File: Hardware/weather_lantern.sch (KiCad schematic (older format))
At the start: 3 parts

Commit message: Added sensors
Added sensors.
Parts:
- added BT?: BATTERY, ~, symbol BATTERY
- added U?: TMP3X, ~, symbol TMP3X
- added U?: HIH-40XX, symbol HIH-40XX
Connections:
- net at U?.19 (IO_29/ADC5/SCLK): now also U?.2 (Vout)
- net at U?.20 (IO_28/ADC4/MISO): now also U?.2 (Vout)
- net at U?.4 (IO_21/PWM_OUT/INT): now also D?.1 (R)
- net at U?.6 (IO_20/PWM/INT): now also D?.2 (G)
- net at U?.7 (IO_19/PWM/AIN0): now also D?.3 (B)
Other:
- moved on the sheet: D?
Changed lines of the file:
@@
 LIBS:valves
 LIBS:Aerodyne_v2
+LIBS:weather_lantern-cache
 EELAYER 27 0
 EELAYER END
@@
 Sheet 1 1
 Title "Weather Lantern"
-Date "6 nov 2013"
+Date "7 nov 2013"
 Rev "1"
 Comp "Aerodyne Labs"
@@
 L DIODE-PHOTO D?
 U 1 1 5279E267
-P 8450 2150
-F 0 "D?" H 8450 2250 60  0000 C CNN
-F 1 "DIODE-PHOTO" H 8450 2050 60  0000 C CNN
-F 2 "~" H 8450 2150 60  0000 C CNN
-F 3 "~" H 8450 2150 60  0000 C CNN
-	1    8450 2150
+P 8950 1700
+F 0 "D?" H 8950 1800 60  0000 C CNN
+F 1 "DIODE-PHOTO" H 8950 1600 60  0000 C CNN
+F 2 "~" H 8950 1700 60  0000 C CNN
+F 3 "~" H 8950 1700 60  0000 C CNN
+	1    8950 1700
 	1    0    0    -1
 $EndComp
@@
 L RGBLED D?
 U 1 1 5279E6DA
-P 8350 3900
-F 0 "D?" H 8350 4200 60  0000 C CNN
-F 1 "RGBLED" H 8350 3600 60  0000 C CNN
-F 2 "" H 8350 3850 60  0000 C CNN
-F 3 "" H 8350 3850 60  0000 C CNN
-	1    8350 3900
+P 3150 3750
+F 0 "D?" H 3150 4050 60  0000 C CNN
+F 1 "RGBLED" H 3150 3450 60  0000 C CNN
+F 2 "" H 3150 3700 60  0000 C CNN
+F 3 "" H 3150 3700 60  0000 C CNN
+	1    3150 3750
 	1    0    0    -1
 $EndComp
+$Comp
+L TMP3X U?
+U 1 1 527B30AF
+P 7900 3250
+F 0 "U?" H 8100 2900 60  0000 C CNN
+F 1 "TMP3X" H 7700 3550 60  0000 C CNN
+F 2 "~" H 7900 3250 60  0000 C CNN
+F 3 "~" H 7900 3250 60  0000 C CNN
+	1    7900 3250
+	-1   0    0    1
+$EndComp
+$Comp
+L HIH-40XX U?
+U 1 1 527B352F
+P 7900 4300
+F 0 "U?" H 7900 4600 60  0000 C CNN
+F 1 "HIH-40XX" H 7900 4000 60  0000 C CNN
+F 2 "" H 7900 4300 60  0000 C CNN
+F 3 "" H 7900 4300 60  0000 C CNN
+	1    7900 4300
+	-1   0    0    1
+$EndComp
+Wire Wire Line
+	3450 3600 3850 3600
+Wire Wire Line
+	3850 3600 3850 3700
+Wire Wire Line
+	3850 3700 4100 3700
+Wire Wire Line
+	3450 3750 3800 3750
+Wire Wire Line
+	3800 3750 3800 3900
+Wire Wire Line
+	3800 3900 4100 3900
+Wire Wire Line
+	3450 3900 3750 3900
+Wire Wire Line
+	3750 3900 3750 4000
+Wire Wire Line
+	3750 4000 4100 4000
+Wire Wire Line
+	7450 4300 6200 4300
+Wire Wire Line
+	7450 3250 7000 3250
+Wire Wire Line
+	7000 3250 7000 4200
+Wire Wire Line
+	7000 4200 6200 4200
+$Comp
+L BATTERY BT?
+U 1 1 527B35BE
+P 5150 2150
+F 0 "BT?" H 5150 2350 50  0000 C CNN
+F 1 "BATTERY" H 5150 1960 50  0000 C CNN
+F 2 "~" H 5150 2150 60  0000 C CNN
+F 3 "~" H 5150 2150 60  0000 C CNN
+	1    5150 2150
+	1    0    0    -1
+$EndComp

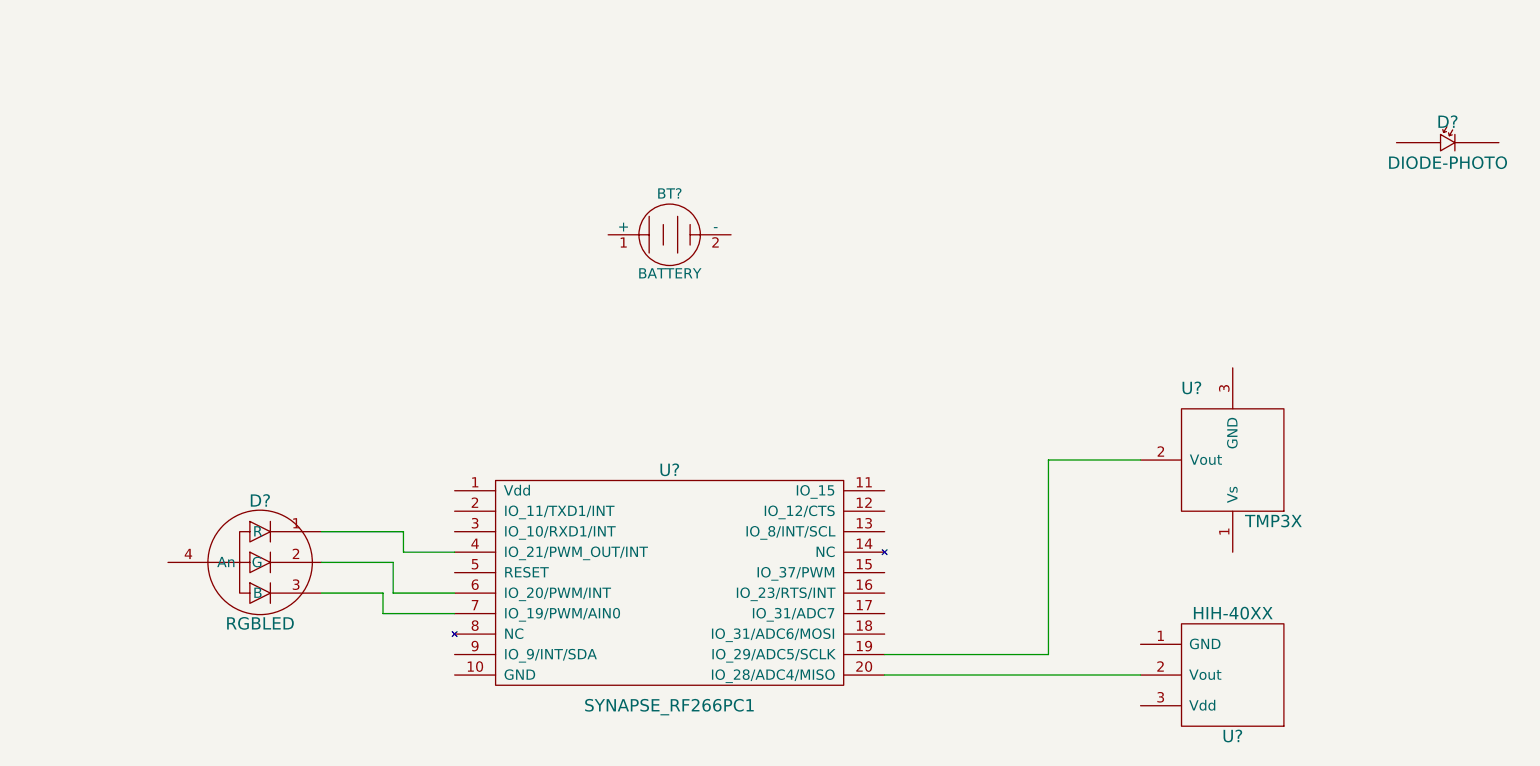
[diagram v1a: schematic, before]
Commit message: Added power supply
Added LDO for power from Li-Ion battery.  Finished wiring temp and
humidity sensor.
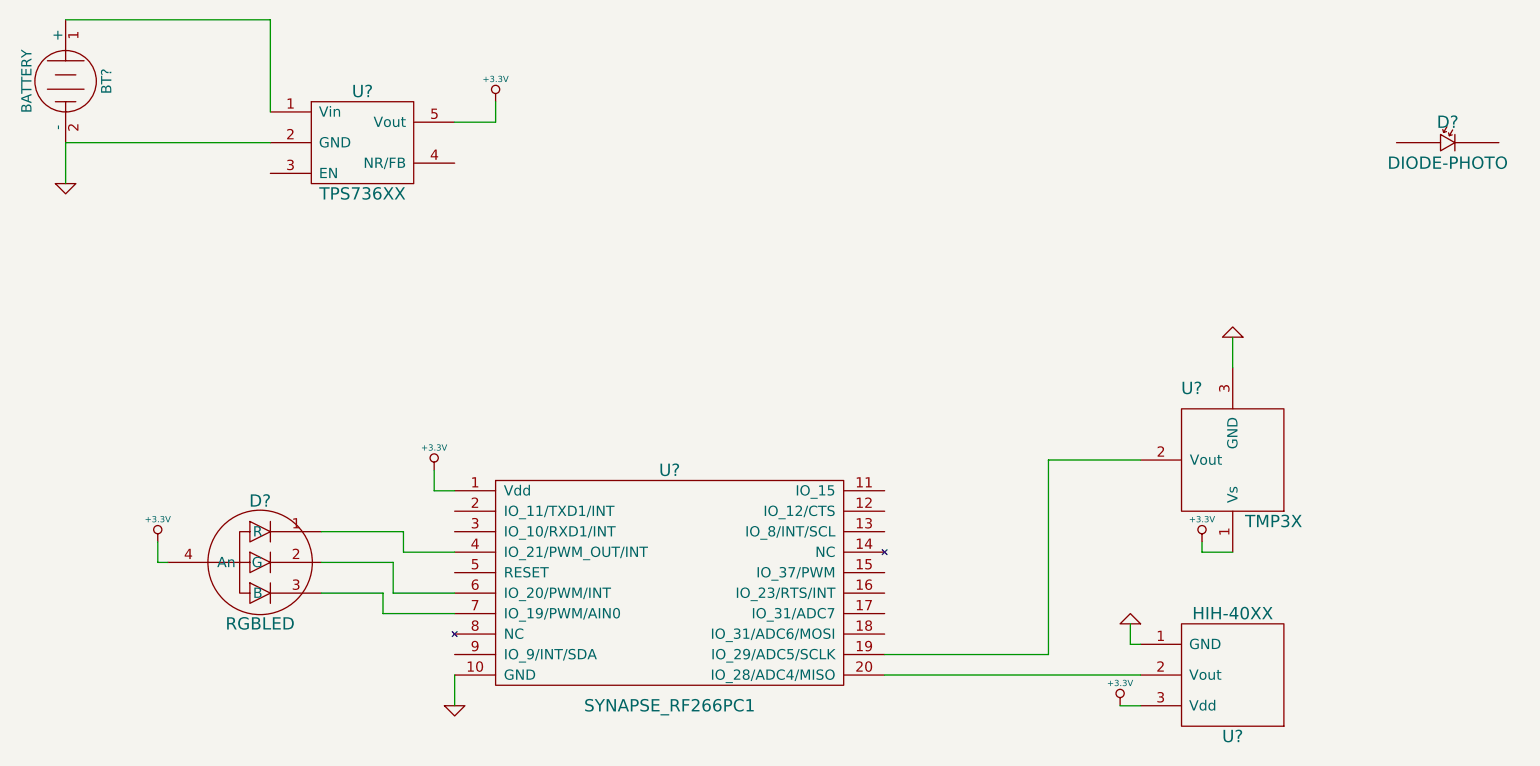
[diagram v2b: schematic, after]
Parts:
- added U?: TPS736XX, symbol TPS736XX
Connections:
- net +3.3V: now reaches U?.1 (Vdd)
- net +3.3V: now also D?.4 (An), U?.1 (Vs), U?.3 (Vdd), U?.5 (Vout)
- net GND: now reaches U?.10 (GND)
- net GND: now also BT?.2 (-), U?.1 (GND), U?.3 (GND), U?.2 (GND)
- net at BT?.1 (+): now also U?.1 (Vin)
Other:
- moved on the sheet: BT?
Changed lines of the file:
@@
 Sheet 1 1
 Title "Weather Lantern"
-Date "7 nov 2013"
+Date "8 nov 2013"
 Rev "1"
 Comp "Aerodyne Labs"
@@
 L BATTERY BT?
 U 1 1 527B35BE
-P 5150 2150
-F 0 "BT?" H 5150 2350 50  0000 C CNN
-F 1 "BATTERY" H 5150 1960 50  0000 C CNN
-F 2 "~" H 5150 2150 60  0000 C CNN
-F 3 "~" H 5150 2150 60  0000 C CNN
-	1    5150 2150
-	1    0    0    -1
-$EndComp
+P 2200 1400
+F 0 "BT?" H 2200 1600 50  0000 C CNN
+F 1 "BATTERY" H 2200 1210 50  0000 C CNN
+F 2 "~" H 2200 1400 60  0000 C CNN
+F 3 "~" H 2200 1400 60  0000 C CNN
+	1    2200 1400
+	0    1    1    0
+$EndComp
+$Comp
+L TPS736XX U?
+U 1 1 527C738C
+P 3650 1700
+F 0 "U?" H 3650 1950 60  0000 C CNN
+F 1 "TPS736XX" H 3650 1450 60  0000 C CNN
+F 2 "" H 3650 1700 60  0000 C CNN
+F 3 "" H 3650 1700 60  0000 C CNN
+	1    3650 1700
+	1    0    0    -1
+$EndComp
+Wire Wire Line
+	2200 1700 3200 1700
+Wire Wire Line
+	2200 1100 3200 1100
+Wire Wire Line
+	3200 1100 3200 1550
+$Comp
+L +3.3V #PWR?
+U 1 1 527C73D1
+P 4300 1500
+F 0 "#PWR?" H 4300 1460 30  0001 C CNN
+F 1 "+3.3V" H 4300 1610 30  0000 C CNN
+F 2 "" H 4300 1500 60  0000 C CNN
+F 3 "" H 4300 1500 60  0000 C CNN
+	1    4300 1500
+	1    0    0    -1
+$EndComp
+Wire Wire Line
+	4100 1600 4300 1600
+Wire Wire Line
+	4300 1600 4300 1500
+$Comp
+L +3.3V #PWR?
+U 1 1 527C73F1
+P 4000 3300
+F 0 "#PWR?" H 4000 3260 30  0001 C CNN
+F 1 "+3.3V" H 4000 3410 30  0000 C CNN
+F 2 "" H 4000 3300 60  0000 C CNN
+F 3 "" H 4000 3300 60  0000 C CNN
+	1    4000 3300
+	1    0    0    -1
+$EndComp
+Wire Wire Line
+	4100 3400 4000 3400
+Wire Wire Line
+	4000 3400 4000 3300
+$Comp
+L GND #PWR?
+U 1 1 527C7413
+P 2200 1900
+F 0 "#PWR?" H 2200 1900 30  0001 C CNN
+F 1 "GND" H 2200 1830 30  0001 C CNN
+F 2 "" H 2200 1900 60  0000 C CNN
+F 3 "" H 2200 1900 60  0000 C CNN
+	1    2200 1900
+	1    0    0    -1
+$EndComp
+Wire Wire Line
+	2200 1700 2200 1900
+Wire Wire Line
+	4100 4300 4100 4450
+$Comp
+L GND #PWR?
+U 1 1 527C744E
+P 4100 4450
+F 0 "#PWR?" H 4100 4450 30  0001 C CNN
+F 1 "GND" H 4100 4380 30  0001 C CNN
+F 2 "" H 4100 4450 60  0000 C CNN
+F 3 "" H 4100 4450 60  0000 C CNN
+	1    4100 4450
+	1    0    0    -1
+$EndComp
+$Comp
+L +3.3V #PWR?
+U 1 1 527C745D
+P 7750 3650
+F 0 "#PWR?" H 7750 3610 30  0001 C CNN
+F 1 "+3.3V" H 7750 3760 30  0000 C CNN
+F 2 "" H 7750 3650 60  0000 C CNN
+F 3 "" H 7750 3650 60  0000 C CNN
+	1    7750 3650
+	1    0    0    -1
+$EndComp
+$Comp
+L +3.3V #PWR?
+U 1 1 527C746C
+P 7350 4450
+F 0 "#PWR?" H 7350 4410 30  0001 C CNN
+F 1 "+3.3V" H 7350 4560 30  0000 C CNN
+F 2 "" H 7350 4450 60  0000 C CNN
+F 3 "" H 7350 4450 60  0000 C CNN
+	1    7350 4450
+	1    0    0    -1
+$EndComp
+$Comp
+L GND #PWR?
+U 1 1 527C747B
+P 7900 2650
+F 0 "#PWR?" H 7900 2650 30  0001 C CNN
+F 1 "GND" H 7900 2580 30  0001 C CNN
+F 2 "" H 7900 2650 60  0000 C CNN
+F 3 "" H 7900 2650 60  0000 C CNN
+	1    7900 2650
+	-1   0    0    1
+$EndComp
+$Comp
+L GND #PWR?
+U 1 1 527C748A
+P 7400 4050
+F 0 "#PWR?" H 7400 4050 30  0001 C CNN
+F 1 "GND" H 7400 3980 30  0001 C CNN
+F 2 "" H 7400 4050 60  0000 C CNN
+F 3 "" H 7400 4050 60  0000 C CNN
+	1    7400 4050
+	-1   0    0    1
+$EndComp
+Wire Wire Line
+	7900 2800 7900 2650
+Wire Wire Line
+	7450 4150 7400 4150
+Wire Wire Line
+	7400 4150 7400 4050
+Wire Wire Line
+	7450 4450 7350 4450
+Wire Wire Line
+	7900 3700 7750 3700
+Wire Wire Line
+	7750 3700 7750 3650
+Wire Wire Line
+	2700 3750 2650 3750
+Wire Wire Line
+	2650 3750 2650 3650
+$Comp
+L +3.3V #PWR?
+U 1 1 527C7532
+P 2650 3650
+F 0 "#PWR?" H 2650 3610 30  0001 C CNN
+F 1 "+3.3V" H 2650 3760 30  0000 C CNN
+F 2 "" H 2650 3650 60  0000 C CNN
+F 3 "" H 2650 3650 60  0000 C CNN
+	1    2650 3650
+	1    0    0    -1
+$EndComp

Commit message: Minor update
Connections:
- net at BT?.1 (+), U?.1 (Vin): now also U?.3 (EN)
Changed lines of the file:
@@
 	1    0    0    -1
 $EndComp
+Wire Wire Line
+	3200 1850 3000 1850
+Wire Wire Line
+	3000 1850 3000 1100
+Connection ~ 3000 1100
 $EndSCHEMATC
